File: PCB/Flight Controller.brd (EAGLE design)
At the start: 34.3 x 47.9 mm, 28 parts, among them J1 ZX62-AB-5PA(31), J2 M50-3600542R, U1 BMP390L, U2 NINA-B306, U3 LMS8117ADT-3.3, U4 BNO055

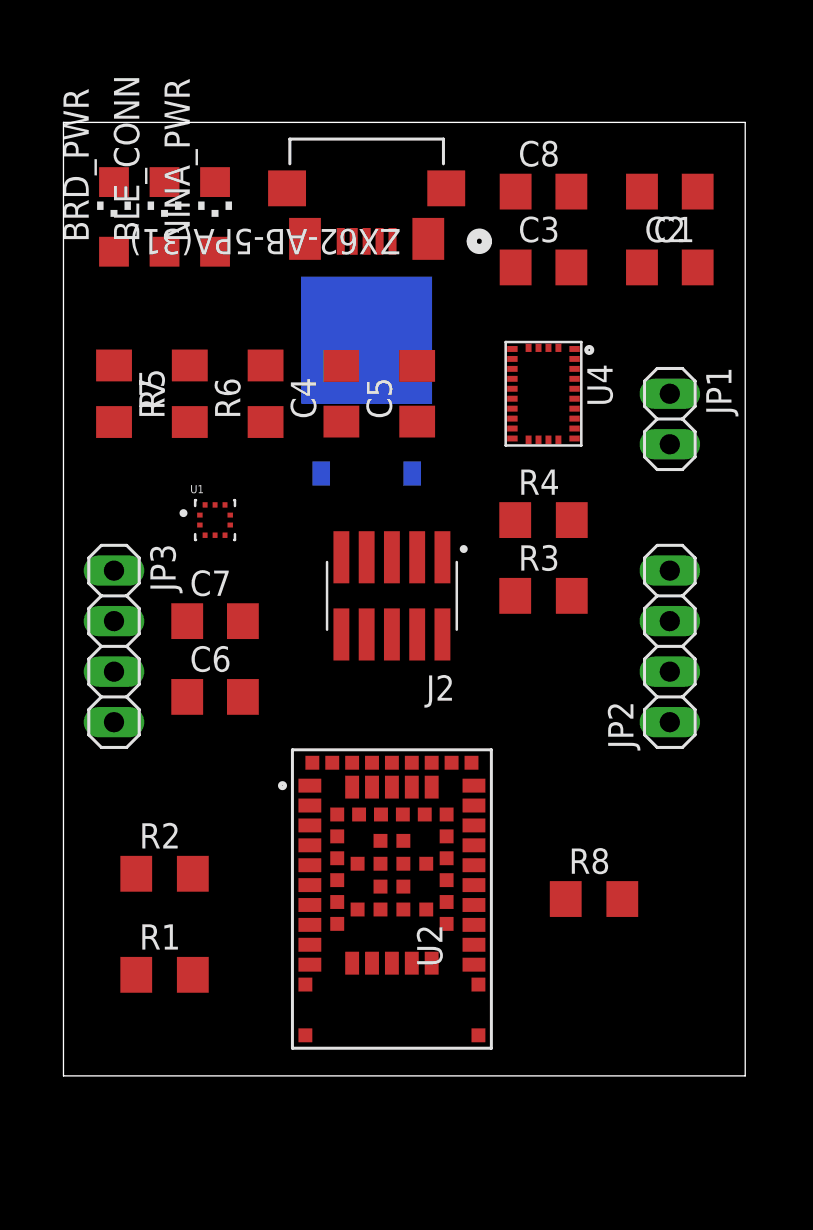
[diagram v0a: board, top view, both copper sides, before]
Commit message: began routing PCB
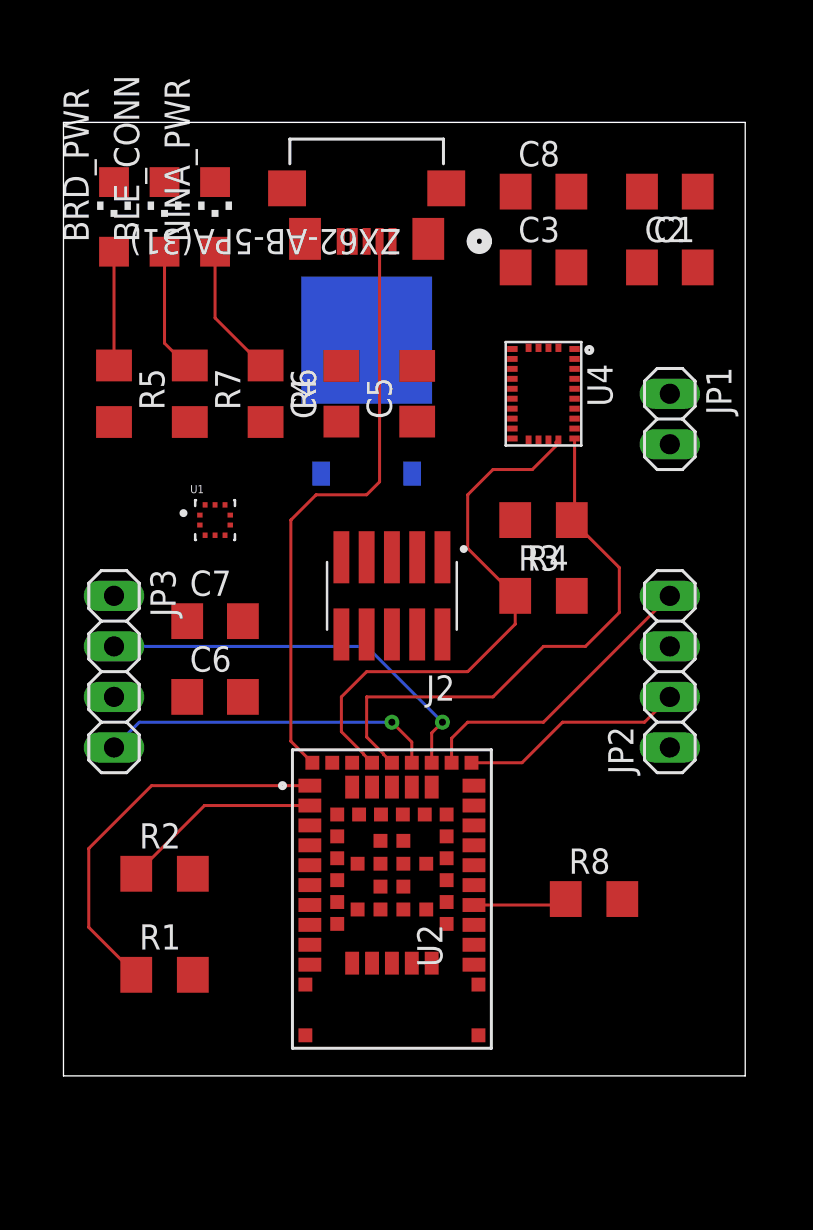
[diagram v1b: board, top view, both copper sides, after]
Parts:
- moved JP2 1.27 mm to (30.5, 20.3)
- moved JP3 1.27 mm to (2.54, 20.3)
- turned R4 to 180 degrees
- turned R6 to 270 degrees
- turned R7 to 270 degrees
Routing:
- net D-: track 0.00 -> 30.0 mm
- net SDA_IMU: track 0.00 -> 28.1 mm
- net SCL_IMU: track 0.00 -> 27.5 mm
- net PWM2: track 0.00 -> 20.4 mm, vias 0 -> 1
- net SCK_AUX: track 0.00 -> 19.8 mm
- net PWM3: track 0.00 -> 17.0 mm, vias 0 -> 1
- net PWM1: track 0.00 -> 15.2 mm
- net PWM0: track 0.00 -> 11.3 mm
- net SDA_AUX: track 0.00 -> 10.1 mm
- net N$2: track 0.00 -> 6.86 mm
- net N$3: track 0.00 -> 6.33 mm
- net N$1: track 0.00 -> 5.72 mm
- net NRESET: track 0.00 -> 4.74 mm

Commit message: continued work on PCB layout and added new headers for UARTs
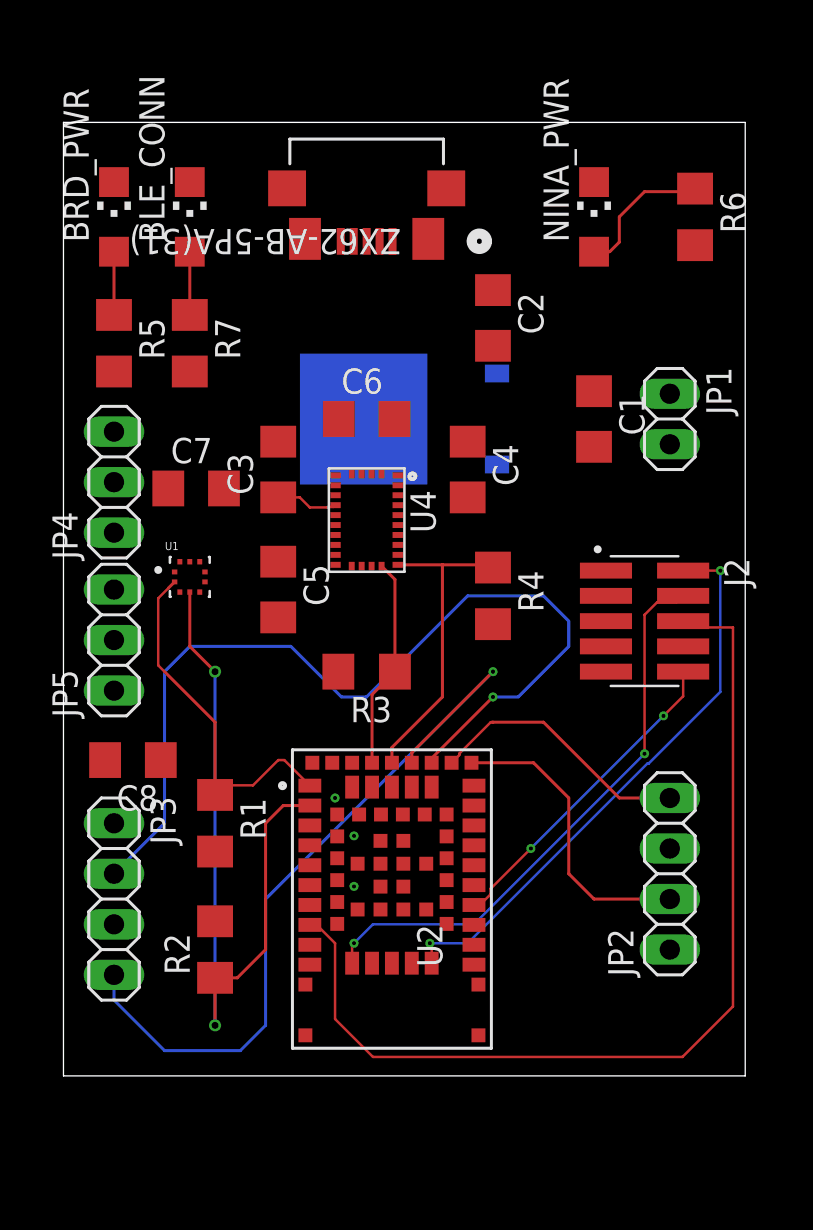
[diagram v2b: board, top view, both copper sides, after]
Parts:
- removed R8: 10k, rcl:R1206
- added JP4, JP5: (no value), pinhead:1X03
- moved C8 35.2 mm to (3.49, 15.9), turned to 180 degrees
- moved R6 23.3 mm to (31.8, 43.2)
- moved NINA_PWR 19.1 mm to (26.7, 43.2)
- moved C3 16.8 mm to (10.8, 30.5), turned to 90 degrees
- moved C6 15.9 mm to (15.2, 33.0)
- moved J2 12.8 mm to (29.2, 22.9), turned to 270 degrees
- moved C5 12.1 mm to (10.8, 24.4), turned to 270 degrees
- moved C1 12.0 mm to (26.7, 33.0), turned to 270 degrees
- moved JP3 11.4 mm to (2.54, 8.89)
- moved U4 10.9 mm to (15.2, 27.9)
- moved JP2 10.2 mm to (30.5, 10.2)
- moved R3 9.67 mm to (15.2, 20.3), turned to 180 degrees
- moved C2 9.25 mm to (21.6, 38.1), turned to 270 degrees
- moved R1 8.03 mm to (7.62, 12.7), turned to 270 degrees
- moved C4 7.41 mm to (20.3, 30.5), turned to 270 degrees
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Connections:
- removed net VCC1: C2.1
- net BMP_INT: now also U2.34; no longer U2.33
- net GND: now also JP4.1, JP5.1
- net NRESET: no longer R8.1
- net UART1_RX: now also JP4.2
- net UART1_TX: now also JP4.3
- net UART2_RX: now also JP5.2
- net UART2_TX: now also JP5.3
- net VDD: now also C2.1; no longer R8.2
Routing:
- net SWO: track 0.00 -> 49.0 mm
- net D-: track 30.0 -> 0.00 mm
- net SWCLK: track 0.00 -> 28.9 mm, vias 0 -> 2
- net SWDIO: track 0.00 -> 28.8 mm, vias 0 -> 2
- net SDA_AUX: track 10.1 -> 36.8 mm, vias 0 -> 2
- net PWM2: track 20.4 -> 46.5 mm
- net PWM3: track 17.0 -> 39.3 mm
- net SCL_IMU: track 27.5 -> 10.6 mm
- net SDA_IMU: track 28.1 -> 15.8 mm
- net NRESET: track 4.74 -> 16.3 mm, vias 0 -> 2
- net PWM0: track 11.3 -> 15.0 mm
- net N$3: track 6.33 -> 3.18 mm
- net N$4: track 0.00 -> 3.14 mm
- net N$1: track 5.72 -> 3.18 mm
- net SCK_AUX: track 19.8 -> 18.1 mm
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
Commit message: PCB signals routed, only power and ground planes left
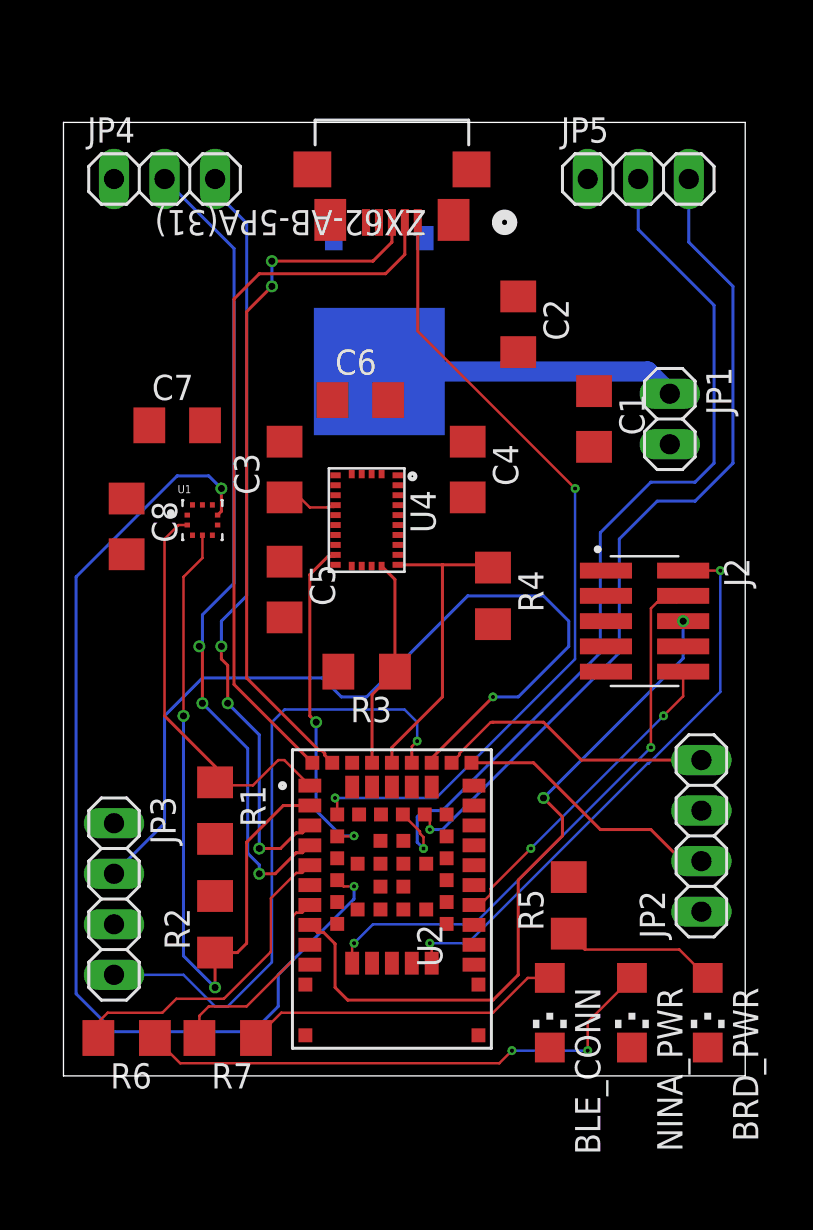
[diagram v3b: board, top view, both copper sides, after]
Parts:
- moved R6 50.2 mm to (3.17, 1.91), turned to 180 degrees
- moved BRD_PWR 49.9 mm to (32.4, 3.17), turned to 180 degrees
- moved BLE_CONN 43.9 mm to (24.4, 3.17), turned to 180 degrees
- moved NINA_PWR 40.1 mm to (28.6, 3.17), turned to 180 degrees
- moved R5 36.3 mm to (25.4, 8.57), turned to 90 degrees
- moved JP5 35.1 mm to (28.9, 45.1), turned to 0 degrees
- moved R7 35.0 mm to (8.26, 1.91), turned to 180 degrees
- moved JP4 15.5 mm to (5.08, 45.1), turned to 0 degrees
- moved C8 11.8 mm to (3.17, 27.6), turned to 270 degrees
- moved C7 3.31 mm to (5.71, 32.7)
- moved U1 2.93 mm to (6.99, 27.9)
- moved U3 2.62 mm to (15.9, 35.6), turned to 180 degrees
- moved JP2 2.48 mm to (32.1, 12.1)
- moved J1 1.59 mm to (16.5, 45.4)
- moved C2 1.31 mm to (22.9, 37.8)
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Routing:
- net BMP_INT: track 0.00 -> 52.1 mm, vias 1 -> 2
- net UART2_RX: track 0.00 -> 45.5 mm, vias 0 -> 1
- net UART2_TX: track 0.00 -> 42.3 mm, vias 0 -> 1
- net UART1_RX: track 0.00 -> 41.5 mm, vias 0 -> 3
- net VBUS: track 0.00 -> 41.1 mm, vias 1 -> 2
- net UART1_TX: track 0.00 -> 38.7 mm, vias 0 -> 3
- net D-: track 0.00 -> 36.1 mm
- net D+: track 0.00 -> 35.0 mm, vias 0 -> 2
- net N$2: track 7.14 -> 27.6 mm, vias 0 -> 2
- net BNO_INT: track 0.00 -> 17.0 mm, vias 1 -> 2
- net PWR_LED: track 0.00 -> 16.3 mm
- net VCC: track 0.00 -> 15.1 mm
- net N$3: track 3.18 -> 16.0 mm
- net SWO: track 49.0 -> 36.6 mm, vias 0 -> 2
- net BLE_LED: track 0.00 -> 10.3 mm
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
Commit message: replaced voltage regulator with SOT-223 package, reviewed board and is ready to order
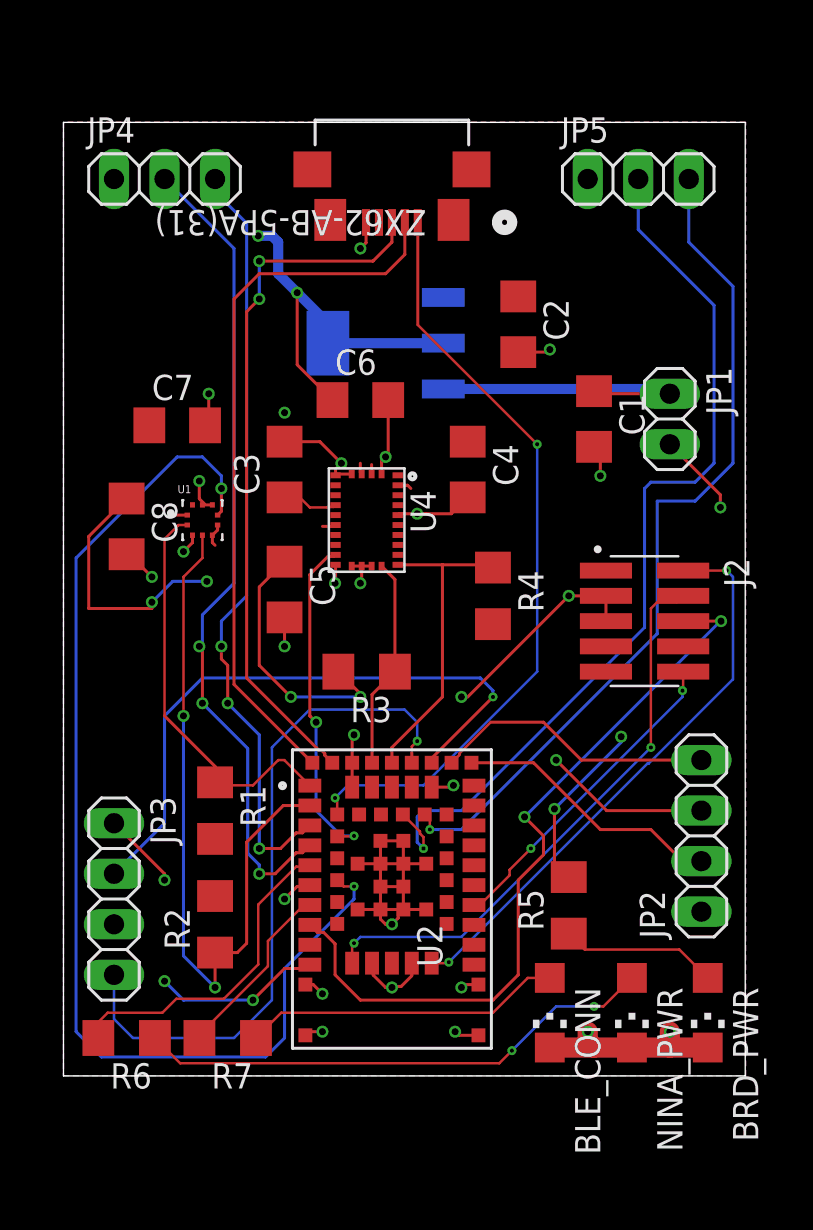
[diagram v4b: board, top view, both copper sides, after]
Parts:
- removed U3: LMS8117ADT-3.3, LMS8117ADT-3.3:TO457P970X238-3N
- added U5: LMS8117AMP-3.3/NOPB, LMS8117AMP-3.3_NOPB:SOT230P700X180-4N
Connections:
- net GND: now also U5.1; no longer U3.2
- net VCC: now also U5.3; no longer U3.3
- net VDD: now also U5.2, U5.4; no longer U3.1
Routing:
- net GND: track 0.00 -> 96.1 mm, vias 0 -> 29
- net VDD: track 0.00 -> 67.1 mm, vias 0 -> 10
- net PWM2: track 43.8 -> 31.5 mm
- net BMP_INT: track 52.1 -> 57.1 mm
- net PWM3: track 31.6 -> 34.6 mm
- net VBUS: track 41.1 -> 38.7 mm
- net SWO: track 36.6 -> 38.2 mm
- net N$2: track 27.6 -> 26.3 mm
- net BLE_LED: track 10.3 -> 9.16 mm
- net UART2_RX: track 45.5 -> 46.1 mm
- net UART2_TX: track 42.3 -> 42.8 mm
- added copper zone on layer 16, net GND
- added copper zone on layer 1, net VDD
